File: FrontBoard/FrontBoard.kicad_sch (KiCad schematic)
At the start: 17 parts

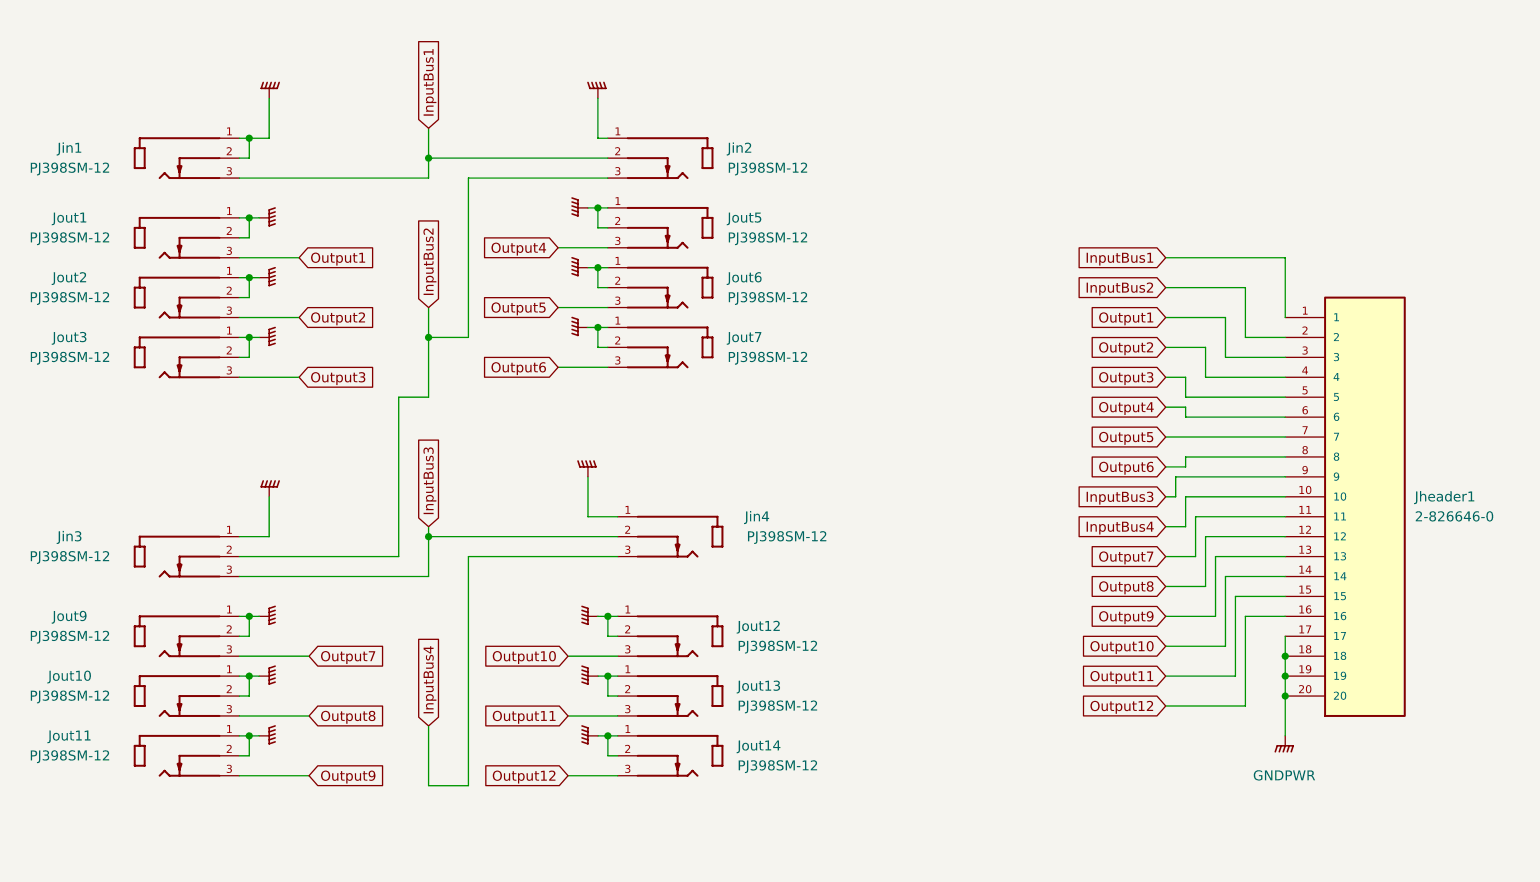
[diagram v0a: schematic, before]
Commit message: added 1M shunt on 1st input so op-amp inputs aren't floating when no signal is plugged in.  Added 100k input resistors to each input. Updated ground to standard GND symbol. Added plot diretory to store ngspice hardcopy plots.
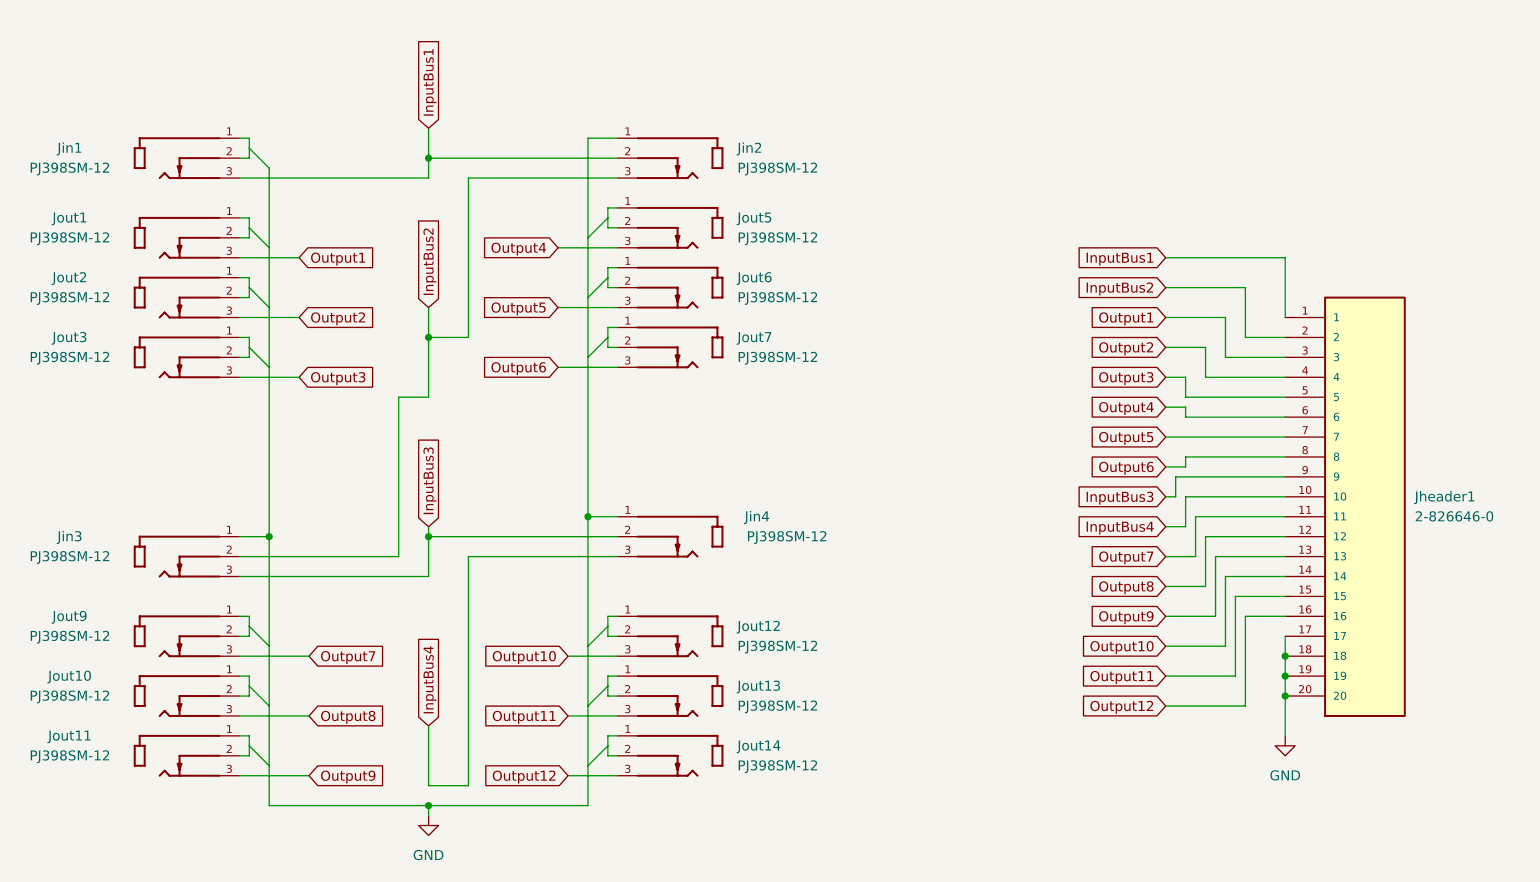
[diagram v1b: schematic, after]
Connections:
- removed net GNDPWR: Jheader1.17, Jheader1.18, Jheader1.19, Jheader1.20, Jin1.1, Jin1.2, Jin2.1, Jin3.1, Jin4.1, Jout1.1, Jout1.2, Jout10.1, Jout10.2, Jout11.1, Jout11.2, Jout12.1, Jout12.2, Jout13.1, Jout13.2, Jout14.1, Jout14.2, Jout2.1, Jout2.2, Jout3.1, Jout3.2, Jout5.1, Jout5.2, Jout6.1, Jout6.2, Jout7.1, Jout7.2, Jout9.1, Jout9.2
- new net: Jout3.1, Jout3.2
- new net: Jout7.1, Jout7.2
- new net: Jout11.1, Jout11.2
- new net: Jout14.1, Jout14.2
- new net: Jout9.1, Jout9.2
- new net: Jout2.1, Jout2.2
- new net: Jout6.1, Jout6.2
- new net: Jin1.1, Jin1.2
- new net: Jout5.1, Jout5.2
- new net: Jout12.1, Jout12.2
- new net: Jout10.1, Jout10.2
- new net: Jout1.1, Jout1.2
- new net: Jout13.1, Jout13.2
- new net GND: Jheader1.17, Jheader1.18, Jheader1.19, Jheader1.20, Jin2.1, Jin3.1, Jin4.1
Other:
- moved on the sheet: Jin2, Jout5, Jout6, Jout7

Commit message: updated power supply
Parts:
- Jheader1: footprint TE_2-826646-0 -> 2-826646-0:TE_2-826646-0
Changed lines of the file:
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@@
       (effects (font (size 1.27 1.27)) (justify left))
     )
-    (property "Footprint" "TE_2-826646-0" (id 2) (at 252.73 100.33 0)
+    (property "Footprint" "2-826646-0:TE_2-826646-0" (id 2) (at 252.73 100.33 0)
       (effects (font (size 1.27 1.27)) (justify bottom) hide)
     )

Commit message: remove simulation.  added project level symbols and footprints
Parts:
- Jheader1: Spice_Model 2-826646-0 -> (none); Spice_Netlist_Enabled N -> (none); Spice_Primitive J -> (none)
- Jin1, Jin2, Jin3, Jin4, Jout1, Jout10, Jout11, Jout12, Jout13, Jout14, Jout2, Jout3, Jout5, Jout6, Jout7, Jout9: Spice_Model PJ398SM-12 -> (none); Spice_Netlist_Enabled N -> (none); Spice_Primitive J -> (none)

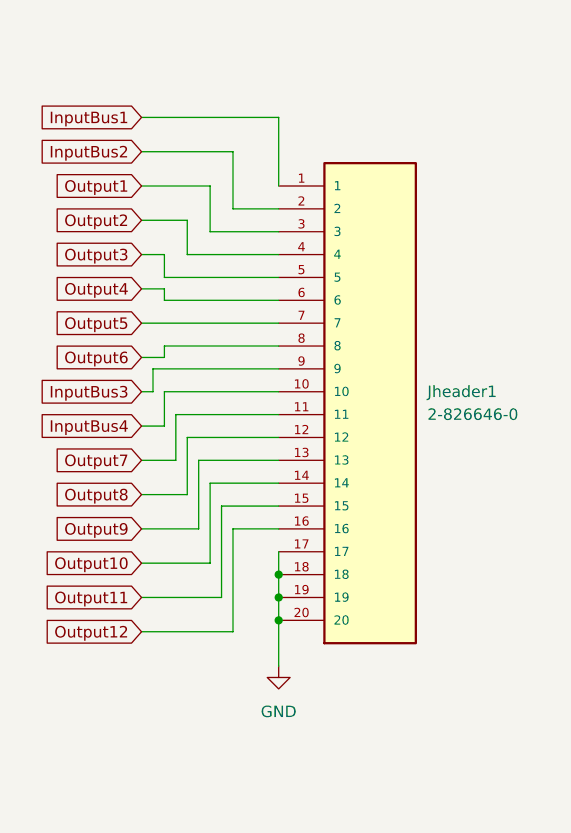
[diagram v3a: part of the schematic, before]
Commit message: updated with new footprints and 3d models
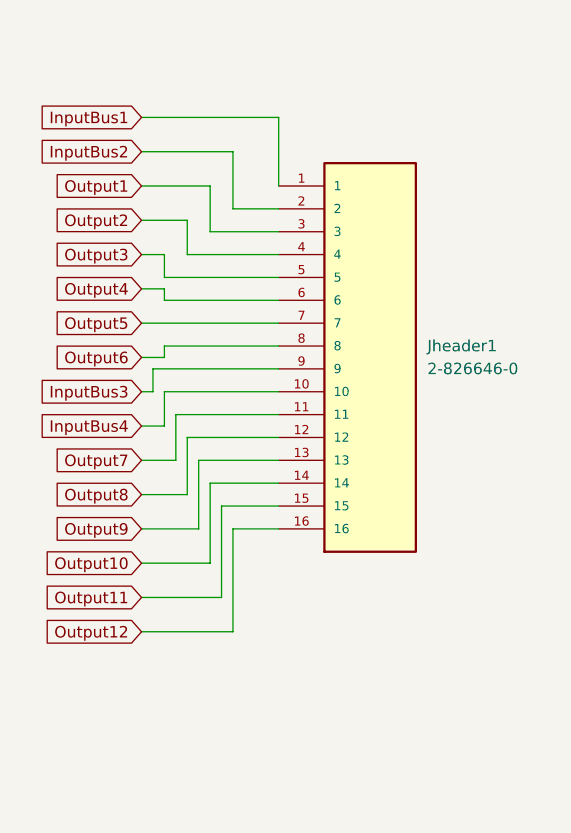
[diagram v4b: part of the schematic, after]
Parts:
- Jheader1: footprint 2-826646-0:TE_2-826646-0 -> TE_1-826936-6:TE_1-826936-6; symbol 2-826646-0:2-826646-0 -> 1-826936-6:1-826936-6; Centerline_Pitch (none) -> 2.54 mm[.1 in]; Comment 2-826646-0 -> 1-826936-6; Number_of_Positions (none) -> 16; Product_Type (none) -> Connector
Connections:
- net GND: no longer Jheader1.17, Jheader1.18, Jheader1.19, Jheader1.20

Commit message: updated placement
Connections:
- net Output10: now also Jheader1.8; no longer Jheader1.14
- net Output5: now also Jheader1.12; no longer Jheader1.7
- net Output6: now also Jheader1.14; no longer Jheader1.8
- net Output8: now also Jheader1.13; no longer Jheader1.12
- net Output9: now also Jheader1.7; no longer Jheader1.13
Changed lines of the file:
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@@
     )
   )
-  (global_label "Output10" (shape input) (at 227.33 116.84 180) (fields_autoplaced)
+  (global_label "Output10" (shape input) (at 227.33 93.98 180) (fields_autoplaced)
     (effects (font (size 1.27 1.27)) (justify right))
-    (property "Intersheetrefs" "${INTERSHEET_REFS}" (at 216.2688 116.9194 0)
+    (property "Intersheetrefs" "${INTERSHEET_REFS}" (at 216.2688 94.0594 0)
       (effects (font (size 1.27 1.27)) (justify right) hide)
     )
@@
     )
   )
-  (global_label "Output9" (shape input) (at 227.33 113.03 180) (fields_autoplaced)
+  (global_label "Output9" (shape input) (at 227.33 90.17 180) (fields_autoplaced)
     (effects (font (size 1.27 1.27)) (justify right))
-    (property "Intersheetrefs" "${INTERSHEET_REFS}" (at 217.4783 113.1094 0)
+    (property "Intersheetrefs" "${INTERSHEET_REFS}" (at 217.4783 90.2494 0)
       (effects (font (size 1.27 1.27)) (justify right) hide)
     )
@@
     )
   )
-  (global_label "Output8" (shape input) (at 227.33 109.22 180) (fields_autoplaced)
+  (global_label "Output8" (shape input) (at 227.33 113.03 180) (fields_autoplaced)
     (effects (font (size 1.27 1.27)) (justify right))
-    (property "Intersheetrefs" "${INTERSHEET_REFS}" (at 217.4783 109.1406 0)
+    (property "Intersheetrefs" "${INTERSHEET_REFS}" (at 217.4783 112.9506 0)
       (effects (font (size 1.27 1.27)) (justify right) hide)
     )
@@
     )
   )
-  (global_label "Output6" (shape input) (at 227.33 93.98 180) (fields_autoplaced)
+  (global_label "Output6" (shape input) (at 227.33 116.84 180) (fields_autoplaced)
     (effects (font (size 1.27 1.27)) (justify right))
-    (property "Intersheetrefs" "${INTERSHEET_REFS}" (at 217.4783 93.9006 0)
+    (property "Intersheetrefs" "${INTERSHEET_REFS}" (at 217.4783 116.7606 0)
       (effects (font (size 1.27 1.27)) (justify right) hide)
     )
@@
     )
   )
-  (global_label "Output5" (shape input) (at 227.33 90.17 180) (fields_autoplaced)
+  (global_label "Output5" (shape input) (at 227.33 109.22 180) (fields_autoplaced)
     (effects (font (size 1.27 1.27)) (justify right))
-    (property "Intersheetrefs" "${INTERSHEET_REFS}" (at 217.4783 90.0906 0)
+    (property "Intersheetrefs" "${INTERSHEET_REFS}" (at 217.4783 109.1406 0)
       (effects (font (size 1.27 1.27)) (justify right) hide)
     )

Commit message: first pass at routing mainboard
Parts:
- Jheader1: footprint TE_1-826936-6:TE_1-826936-6 -> SAMTEC_ESQ-120-12-T-S; symbol 1-826936-6:1-826936-6 -> ESQ-120-12-T-S:ESQ-120-12-T-S; MANUFACTURER (none) -> Samtec; PARTREV (none) -> R; STANDARD (none) -> Manufacturer Recommendations
- renumbered Jout12 to Jout10, Jout13 to Jout11, Jout14 to Jout12, Jout5 to Jout4, Jout6 to Jout5, Jout7 to Jout6, Jout9 to Jout7, Jout10 to Jout8, Jout11 to Jout9
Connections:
- net GND: now also Jheader1.17, Jheader1.18, Jheader1.19, Jheader1.20
- net InputBus1: now also Jheader1.01; no longer Jheader1.1
- net InputBus2: now also Jheader1.02; no longer Jheader1.2
- net InputBus3: now also Jheader1.09; no longer Jheader1.9
- net Output1: now also Jheader1.03; no longer Jheader1.3
- net Output10: now also Jheader1.08; no longer Jheader1.8
- net Output2: now also Jheader1.04; no longer Jheader1.4
- net Output3: now also Jheader1.05; no longer Jheader1.5
- net Output4: now also Jheader1.06; no longer Jheader1.6
- net Output9: now also Jheader1.07; no longer Jheader1.7

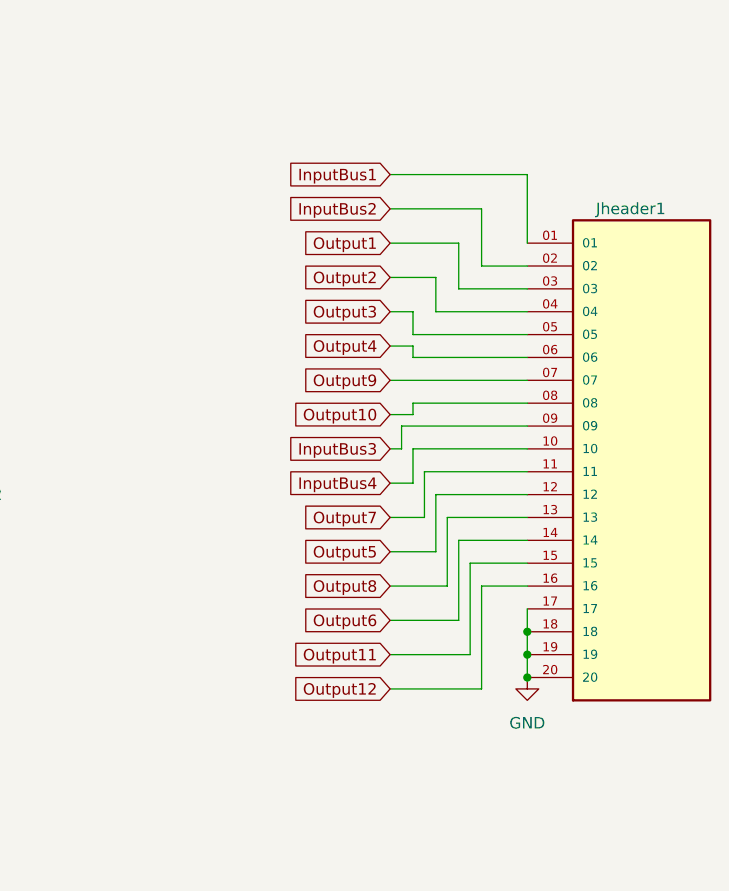
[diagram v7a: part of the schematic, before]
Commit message: fixed incorrect routing on Jheader1, moved silk screens to back layer for easy readability after assembly, oriented all jacks in the upright postition to solvealignnment descrepency in 3d model vs gerber print
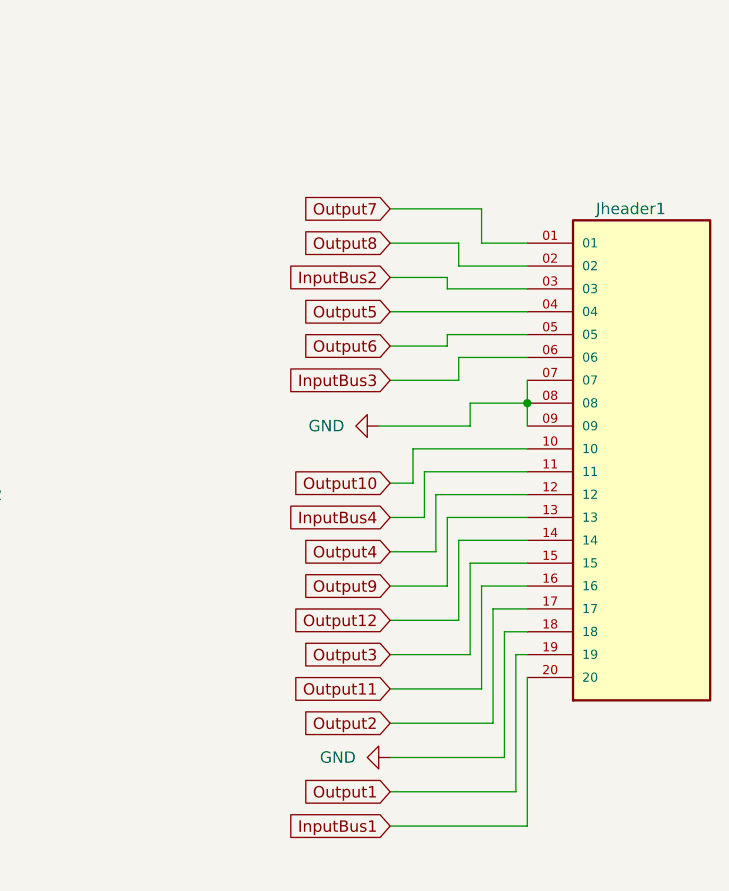
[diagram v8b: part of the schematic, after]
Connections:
- net GND: now also Jheader1.07, Jheader1.08, Jheader1.09; no longer Jheader1.17, Jheader1.19, Jheader1.20
- net InputBus1: now also Jheader1.20; no longer Jheader1.01
- net InputBus2: now also Jheader1.03; no longer Jheader1.02
- net InputBus3: now also Jheader1.06; no longer Jheader1.09
- net InputBus4: now also Jheader1.11; no longer Jheader1.10
- net Output1: now also Jheader1.19; no longer Jheader1.03
- net Output10: now also Jheader1.10; no longer Jheader1.08
- net Output11: now also Jheader1.16; no longer Jheader1.15
- net Output12: now also Jheader1.14; no longer Jheader1.16
- net Output2: now also Jheader1.17; no longer Jheader1.04
- net Output3: now also Jheader1.15; no longer Jheader1.05
- net Output4: now also Jheader1.12; no longer Jheader1.06
- net Output5: now also Jheader1.04; no longer Jheader1.12
- net Output6: now also Jheader1.05; no longer Jheader1.14
- net Output7: now also Jheader1.01; no longer Jheader1.11
- net Output8: now also Jheader1.02; no longer Jheader1.13
- net Output9: now also Jheader1.13; no longer Jheader1.07
